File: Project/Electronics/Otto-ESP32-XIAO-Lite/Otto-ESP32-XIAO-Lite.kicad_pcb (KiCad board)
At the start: 2 copper layers, 60 x 52 mm, 54 parts, among them J1 Conn_01x03, J10 Conn_01x02, J12 OLED 0,91" - I2C (SKU21796), J13 MPU6050, J2 Conn_01x03, J3 Conn_01x03, J4 Conn_01x03, J5 Conn_01x03, J6 Conn_01x03, J7 Conn_01x04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

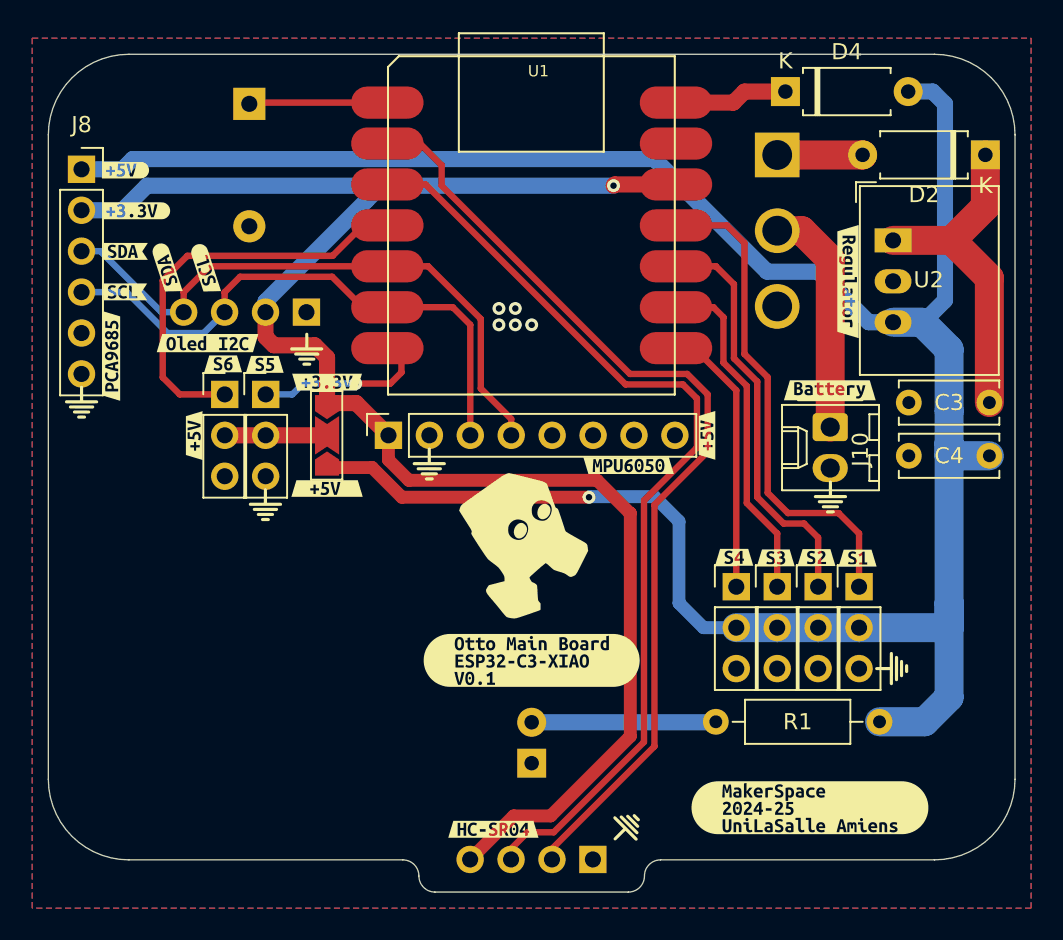
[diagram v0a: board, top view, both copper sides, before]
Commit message: add qrCode - clean PCB
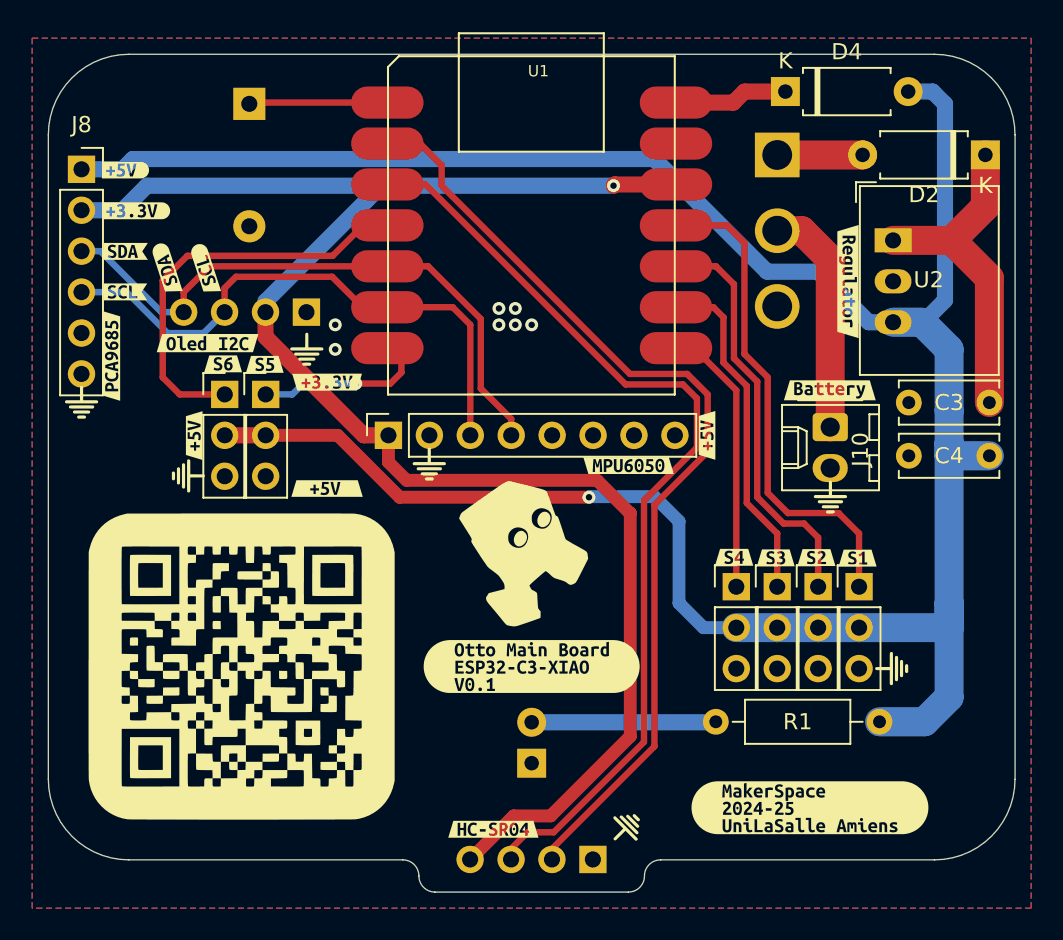
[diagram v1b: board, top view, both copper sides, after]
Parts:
- removed JP1: SolderJumper_3_Open, Jumper:SolderJumper-3_P2.0mm_Open_TrianglePad1.0x1.5mm_NumberLabels
- added G***: LOGO, LOGO, F.Cu at (112.0, 88.0)
- moved G*** 5.11 mm to (108.7, 76.2), turned to -90 degrees
- moved G*** 0.49 mm to (129.5, 81.0)
- moved kibuzzard-6707CF99 0.38 mm to (130.0, 88.0)
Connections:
- J5 pad 2: Net-(J5-Pin_2) -> +5V
- J6 pad 2: Net-(J5-Pin_2) -> +5V
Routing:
- net +5V: track 154.6 -> 161.8 mm
- net Net-(J5-Pin_2): track 6.35 -> 0.00 mm
- net +3.3V: track 105.7 -> 104.2 mm
- net GND: vias 5 -> 7
